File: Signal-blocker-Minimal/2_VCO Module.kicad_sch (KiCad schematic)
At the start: 5 parts

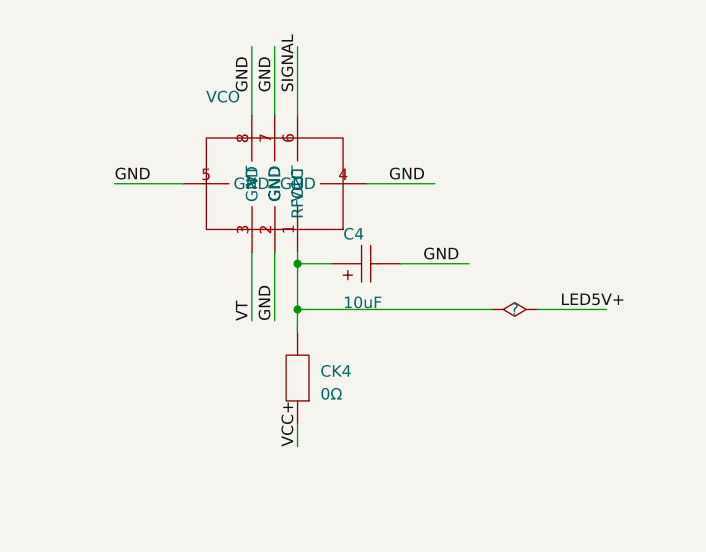
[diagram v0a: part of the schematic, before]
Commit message: Version 2.1 Update！
Fix some circuit!
More stabler!
Replace all the restrictor and capacitor into 0603 packaging!
create BOM excel,Bill of Material.
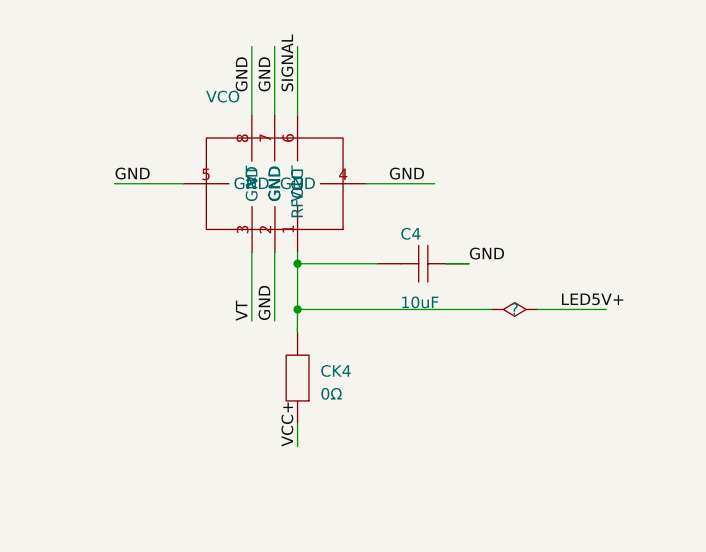
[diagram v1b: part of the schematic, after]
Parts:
- removed ?: (no value), ProPrj_Sig-easyedapro:, symbol ProPrj_Sig-easyedapro:Drawing-Symbol_A4
- removed ?: (no value), ProPrj_Sig-easyedapro:, symbol ProPrj_Sig-easyedapro:Short-Symbol
- removed C4: 10uF, ProPrj_Sig-easyedapro:CAP-SMD_L3.2-W1.6-RD-C7171, symbol ProPrj_Sig-easyedapro:TAJA106K016RNJ
- removed CK4: 0Ω, ProPrj_Sig-easyedapro:R0603, symbol ProPrj_Sig-easyedapro:0Ω
- removed VCO: (no value), ProPrj_Sig-easyedapro:1234, symbol ProPrj_Sig-easyedapro:vco
- added ?: (no value), Signal-blo-easyedapro:, symbol Signal-blo-easyedapro:Drawing-Symbol_A4
- added ?: (no value), Signal-blo-easyedapro:, symbol Signal-blo-easyedapro:Short-Symbol
- added C4: 10uF, Signal-blo-easyedapro:C0603, symbol Signal-blo-easyedapro:HGC0603R5106M160NTHJ
- added CK4: 0Ω, Signal-blo-easyedapro:R0603, symbol Signal-blo-easyedapro:0Ω
- added VCO: (no value), Signal-blo-easyedapro:1234, symbol Signal-blo-easyedapro:vco
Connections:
- net GND: now also C4.2, VCO.4 (GND), VCO.5 (GND), VCO.7 (GND)
- net LED5V+: now also ?.2 (Pin1)
- net SIGNAL: now also VCO.6 (RFOUT)
- net VCC+: now also CK4.1
- new net: ?.1 (Pin1), C4.1
